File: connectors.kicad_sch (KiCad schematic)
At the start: 4 parts, among them J1 Conn_01x04_Pin, J2 Conn_01x04_Pin, J3 Conn_01x09_Pin, J4 Conn_02x03_Odd_Even

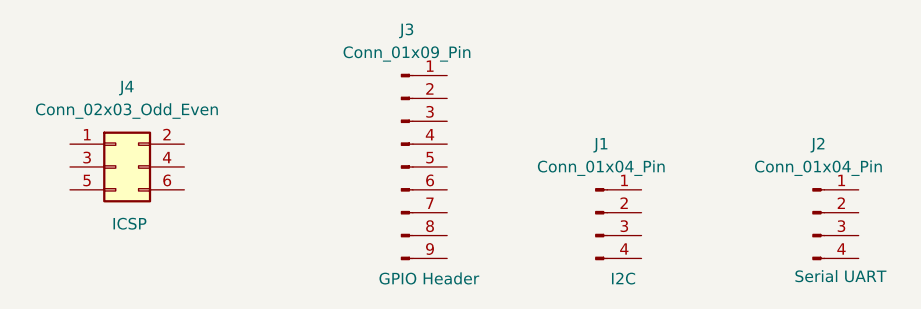
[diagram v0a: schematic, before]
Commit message: Added component values
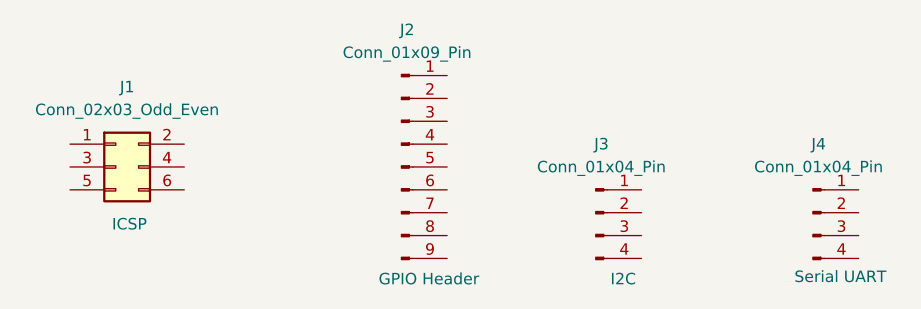
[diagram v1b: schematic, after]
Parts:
- renumbered J4 to J1, J3 to J2, J1 to J3, J2 to J4
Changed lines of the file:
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@@
 		(on_board yes)
 		(dnp no)
-		(property "Reference" "J4"
+		(property "Reference" "J1"
 			(at 86.36 127 0)
 			(effects
@@
 			(project ""
 				(path "/88634b3b-a8f6-4827-a918-596120a151d0/7354aedf-757b-46de-b58d-6907bea158be"
-					(reference "J4")
+					(reference "J1")
 					(unit 1)
 				)
@@
 		(on_board yes)
 		(dnp no)
-		(property "Reference" "J1"
+		(property "Reference" "J3"
 			(at 139.065 133.35 0)
 			(effects
@@
 			(project ""
 				(path "/88634b3b-a8f6-4827-a918-596120a151d0/7354aedf-757b-46de-b58d-6907bea158be"
-					(reference "J1")
+					(reference "J3")
 					(unit 1)
 				)
@@
 		(on_board yes)
 		(dnp no)
-		(property "Reference" "J2"
+		(property "Reference" "J4"
 			(at 163.195 133.35 0)
 			(effects
@@
 			(project ""
 				(path "/88634b3b-a8f6-4827-a918-596120a151d0/7354aedf-757b-46de-b58d-6907bea158be"
-					(reference "J2")
+					(reference "J4")
 					(unit 1)
 				)
@@
 		(on_board yes)
 		(dnp no)
-		(property "Reference" "J3"
+		(property "Reference" "J2"
 			(at 117.475 120.65 0)
 			(effects
@@
 			(project ""
 				(path "/88634b3b-a8f6-4827-a918-596120a151d0/7354aedf-757b-46de-b58d-6907bea158be"
-					(reference "J3")
-					(unit 1)
-				)
+					(reference "J2")
+					(unit 1)
+				)

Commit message: assigned footprints
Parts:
- J1: footprint (none) -> Connector_PinHeader_2.54mm:PinHeader_2x03_P2.54mm_Vertical
- J2: footprint (none) -> Connector_PinHeader_2.54mm:PinHeader_1x09_P2.54mm_Vertical
- J3, J4: footprint (none) -> Connector_PinHeader_2.54mm:PinHeader_1x04_P2.54mm_Vertical
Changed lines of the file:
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@@
 			)
 		)
-		(property "Footprint" ""
+		(property "Footprint" "Connector_PinHeader_2.54mm:PinHeader_2x03_P2.54mm_Vertical"
 			(at 85.09 135.89 0)
 			(effects
@@
 			)
 		)
-		(property "Footprint" ""
+		(property "Footprint" "Connector_PinHeader_2.54mm:PinHeader_1x04_P2.54mm_Vertical"
 			(at 138.43 140.97 0)
 			(effects
@@
 			)
 		)
-		(property "Footprint" ""
+		(property "Footprint" "Connector_PinHeader_2.54mm:PinHeader_1x04_P2.54mm_Vertical"
 			(at 162.56 140.97 0)
 			(effects
@@
 			)
 		)
-		(property "Footprint" ""
+		(property "Footprint" "Connector_PinHeader_2.54mm:PinHeader_1x09_P2.54mm_Vertical"
 			(at 116.84 135.89 0)
 			(effects

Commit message: completed comments
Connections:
- net MISO: now reaches J1.1 (Pin_1)
- net Vcc: now reaches J1.2 (Pin_2)
- net Vcc: now also J2.9 (Pin_9), J3.2 (Pin_2), J4.2 (Pin_2)
- net SCK: now reaches J1.3 (Pin_3)
- net SCK: now also J3.4 (Pin_4)
- net MOSI: now reaches J1.4 (Pin_4)
- net RESET: now reaches J1.5 (Pin_5)
- net GND: now reaches J1.6 (Pin_6)
- net GND: now also J2.8 (Pin_8), J3.1 (Pin_1), J4.1 (Pin_1)
- net SDA: now reaches J3.3 (Pin_3)
- net RX: now reaches J4.3 (Pin_3)
- net TX: now reaches J4.4 (Pin_4)
- net D2: now reaches J2.1 (Pin_1)
- net D3: now reaches J2.2 (Pin_2)
- net D4: now reaches J2.3 (Pin_3)
- net D5: now reaches J2.4 (Pin_4)
- net D6: now reaches J2.5 (Pin_5)
- net D7: now reaches J2.6 (Pin_6)
- net D8: now reaches J2.7 (Pin_7)
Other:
- moved on the sheet: J1, J2, J3, J4
